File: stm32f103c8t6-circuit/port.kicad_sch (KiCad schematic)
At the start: 26 parts, among them J1 Conn_01x04, J1 Conn_01x06, J3 Conn_01x03, J4 Conn_01x02, J4 Conn_01x03, J5 Conn_01x03, J5 USB_C_Receptacle_USB2.0, J6 Conn_01x04, J8 Conn_01x02, SW2 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

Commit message: Modify PCH and SCH
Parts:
- removed D5, D6: LED, LED_SMD:LED_0603_1608Metric, symbol Device:LED
- removed J8: Conn_01x02, Connector_AMASS:AMASS_XT30UPB-M_1x02_P5.0mm_Vertical, symbol 302_Link_W2B-Connector:Conn_01x02
- removed R10, R9: 1K, PCM_001_GN_RCL_SMD:R0603(1608M), symbol 001_Basic_PassiveComponents:001_Resistor
- removed R12, R13: 10k, PCM_001_GN_RCL_SMD:R0603(1608M), symbol 001_Basic_PassiveComponents:001_Resistor
- removed SW2, SW3: (no value), Button_Switch_SMD:SW_SPST_FSMSM, symbol Switch:SW_Push
- J1: footprint PCM_205_CONN_GH_SMD:GH1.25_H_4 -> Connector_PinHeader_2.54mm:PinHeader_1x04_P2.54mm_Vertical
- R11: footprint PCM_001_GN_RCL_SMD:R0603(1608M) -> ResistorSMD:R_0603_1608Metric
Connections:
- net 5V: no longer C18.2, J5.A4 (VBUS), J5.A9 (VBUS), J5.B4 (VBUS), J5.B9 (VBUS), U4.3 (VCC)
- net VCC renamed +3V3
- net i2C1_SCL renamed I2C1_SCL
- net i2C1_SDA renamed I2C1_SDA
- new net +5V: C18.2, J5.A4 (VBUS), J5.A9 (VBUS), J5.B4 (VBUS), J5.B9 (VBUS), U4.3 (VCC)
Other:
- note added: "OLED Moudle"
- note added: "Port"
- note added: "USB to UART"
- moved on the sheet: C17, C18, C19, J1, J3, J4, J5, J6, R11, U4, U5

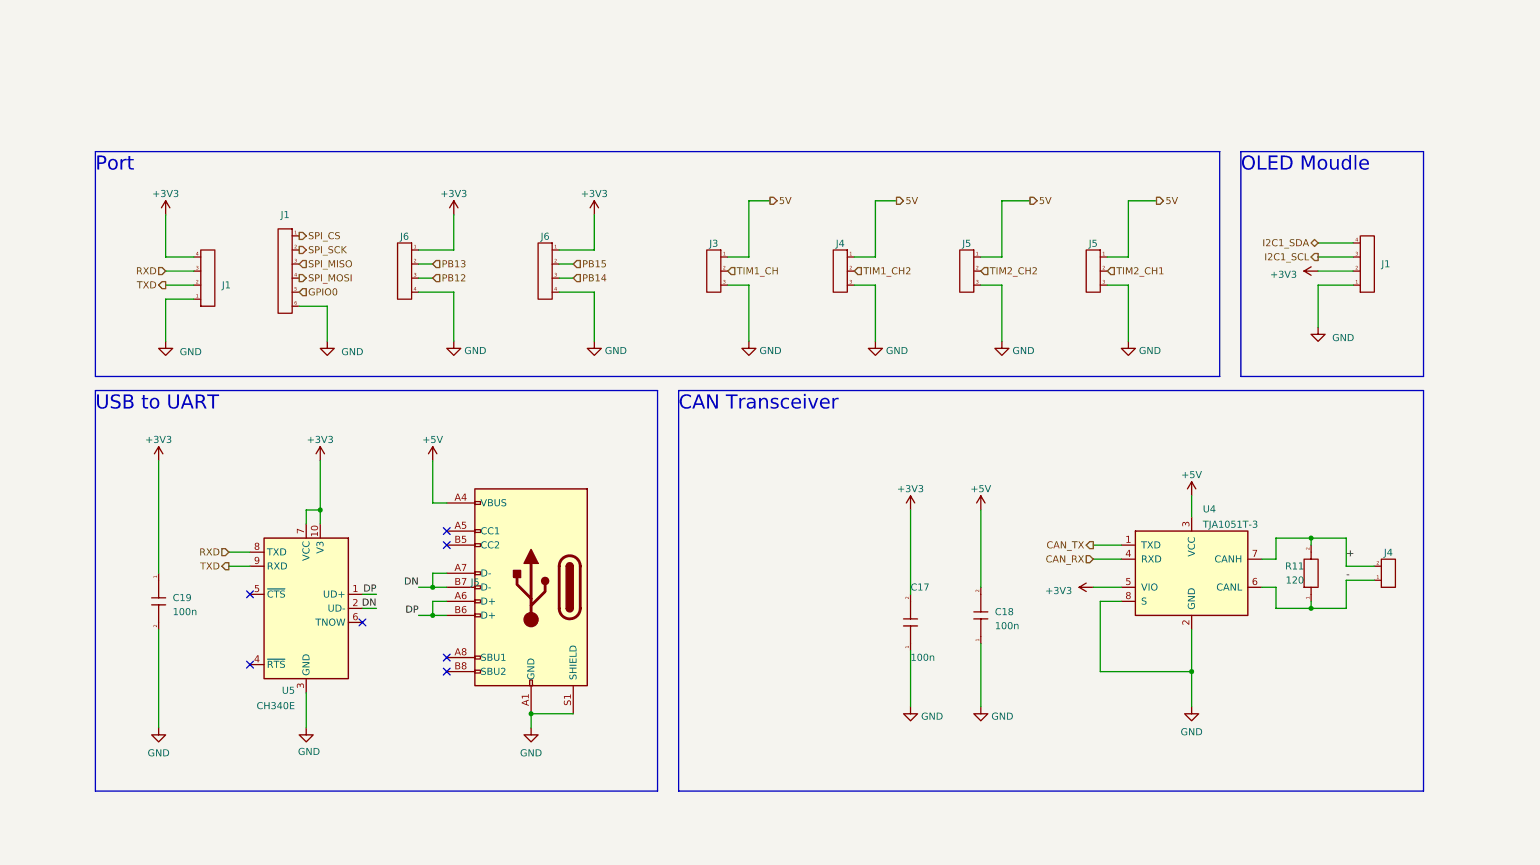
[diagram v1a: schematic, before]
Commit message: Fix some SCH bugs
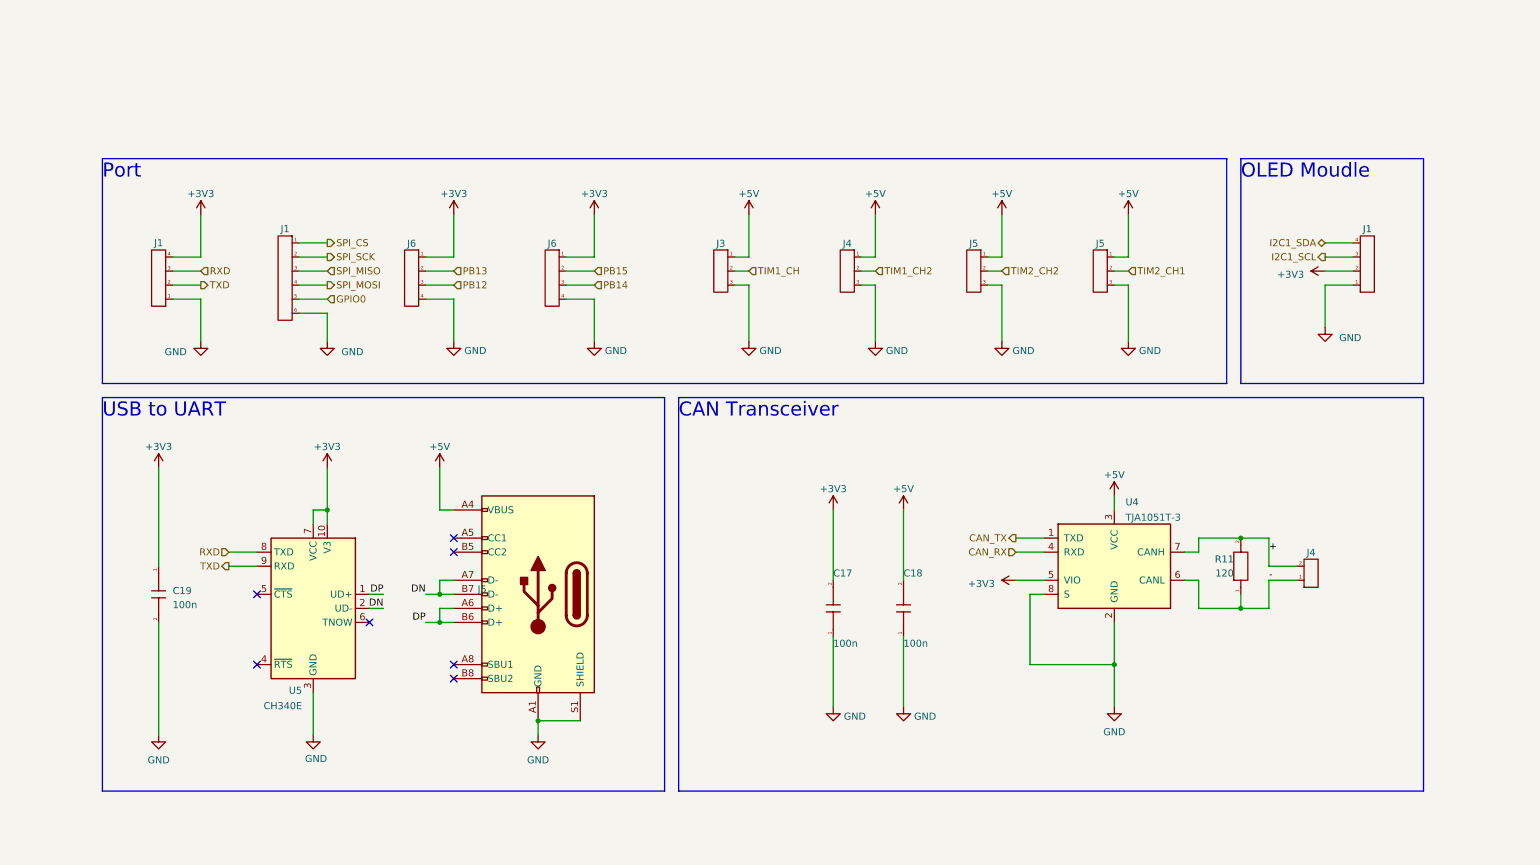
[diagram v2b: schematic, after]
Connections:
- net 5V is gone; now on net +5V: J3.1, J4.1, J5.1, J5.1
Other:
- moved on the sheet: C17, C18, C19, J1, J3, J4, J5, J6, R11, U4, U5
